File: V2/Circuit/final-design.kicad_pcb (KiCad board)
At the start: 2 copper layers, 62.8 x 62.2 mm, 27 parts, among them J1 Conn_02x05_Odd_Even, U1 LM338T, U2 TMC2209_SILENTSTEPSTICK

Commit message: minor changes in circuit and more dev in programming
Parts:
- renumbered StopButton1 to ControlSwitch1, ControlSwitch1 to StopButton1
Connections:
- ControlSwitch1 pad 1: STOP_Button -> control-mode-switch
- MCU1 pad 19: STOP_Button -> control-mode-switch
- MCU1 pad 21: control-mode-switch -> STOP_Button
- StopButton1 pad 1: control-mode-switch -> STOP_Button
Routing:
- net control-mode-switch: track 19.6 -> 6.91 mm
- net STOP_Button: track 6.91 -> 19.6 mm
- net GND: track 357.6 -> 356.7 mm
- net Encoder_button1: track 65.9 -> 66.6 mm

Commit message: minor circuit changes
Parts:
- R4: value 200 -> 150
- R5: value 330 -> 470
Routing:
- net Encoder_DT2: track 17.3 -> 16.2 mm
- net GND: track 356.7 -> 357.4 mm
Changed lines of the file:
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@@
 			)
 		)
-		(property "Value" "200"
+		(property "Value" "150"
 			(at 5.31 0 0)
 			(layer "F.Fab")
@@
 		)
 		(property "Value" "STC8H8K64U_SKDIP28"
-			(at 0.1 -21 0)
+			(at 0 0 90)
 			(unlocked yes)
 			(layer "F.Fab")
@@
 		)
 		(fp_text user "${REFERENCE}"
-			(at -0.2 -19.5 0)
+			(at 0.19 -15.99 0)
 			(unlocked yes)
 			(layer "F.Fab")
@@
 		)
 		(property "Value" "TMC2209_SILENTSTEPSTICK"
-			(at 11.05 11.115 0)
+			(at -1.15 -0.81 90)
 			(layer "F.Fab")
 			(effects
@@
 			)
 		)
-		(property "Value" "330"
+		(property "Value" "470"
 			(at 2.31 0 0)
 			(layer "F.Fab")
@@
 	)
 	(segment
-		(start 151.5 91.25)
-		(end 151.5 80.75)
-		(width 0.8)
-		(layer "F.Cu")
-		(net 1)
-	)
-	(segment
 		(start 121.529899 100.5)
 		(end 121.529899 100.499999)
@@
 	)
 	(segment
+		(start 151.3 91.75)
+		(end 145.669239 91.75)
+		(width 0.8)
+		(layer "F.Cu")
+		(net 1)
+	)
+	(segment
 		(start 146.75 114.25)
 		(end 146.25 114.75)
@@
 	)
 	(segment
-		(start 151.5 93.75)
-		(end 151.5 91.95)
+		(start 145.669239 91.75)
+		(end 143.869239 93.55)
 		(width 0.8)
 		(layer "F.Cu")
@@
 	)
 	(segment
-		(start 144.588478 91.75)
-		(end 142.788478 93.55)
-		(width 0.8)
-		(layer "F.Cu")
-		(net 1)
-	)
-	(segment
 		(start 105.916 95.166)
 		(end 104.95 94.2)
@@
 	)
 	(segment
+		(start 151.5 91.95)
+		(end 151.3 91.75)
+		(width 0.8)
+		(layer "F.Cu")
+		(net 1)
+	)
+	(segment
 		(start 119.75 113)
 		(end 122.69 113)
@@
 	)
 	(segment
+		(start 151.5 91.95)
+		(end 151.5 80.75)
+		(width 0.8)
+		(layer "F.Cu")
+		(net 1)
+	)
+	(segment
 		(start 104.05 76.34)
 		(end 105.65 74.74)
@@
 	)
 	(segment
-		(start 151.3 91.75)
-		(end 144.588478 91.75)
+		(start 134.75 69)
+		(end 136.137358 69)
 		(width 0.8)
 		(layer "F.Cu")
@@
 	)
 	(segment
-		(start 151.5 91.95)
-		(end 151.3 91.75)
+		(start 136.75 84.225)
+		(end 137.225 83.75)
 		(width 0.8)
 		(layer "F.Cu")
@@
 	)
 	(segment
-		(start 142.788478 93.55)
+		(start 143.869239 93.55)
 		(end 139.25 93.55)
 		(width 0.8)
@@
 	)
 	(segment
-		(start 134.75 69)
-		(end 136.137358 69)
-		(width 0.8)
-		(layer "F.Cu")
-		(net 1)
-	)
-	(segment
-		(start 136.75 84.225)
-		(end 137.225 83.75)
-		(width 0.8)
-		(layer "F.Cu")
-		(net 1)
-	)
-	(segment
 		(start 148.75 75.46)
 		(end 146.21 75.46)
@@
 	)
 	(segment
+		(start 151.5 93.75)
+		(end 151.5 91.95)
+		(width 0.8)
+		(layer "F.Cu")
+		(net 1)
+	)
+	(segment
 		(start 105.916 99.342956)
 		(end 105.916 95.166)
@@
 	)
 	(segment
+		(start 146.75 70.25)
+		(end 145.05 68.55)
+		(width 0.8)
+		(layer "F.Cu")
+		(net 14)
+	)
+	(segment
 		(start 104.065 70.35)
 		(end 104.065 69.159874)
@@
 	)
 	(segment
+		(start 145.05 68.55)
+		(end 138.425836 68.55)
+		(width 0.8)
+		(layer "F.Cu")
+		(net 14)
+	)
+	(segment
 		(start 141.76 82.45)
 		(end 136.55 82.45)
@@
 	)
 	(segment
-		(start 137.5 72.75)
-		(end 132.75 77.5)
-		(width 0.8)
-		(layer "F.Cu")
-		(net 14)
-	)
-	(segment
 		(start 121.17 62.70868)
 		(end 121.17 60.714466)
@@
 	)
 	(segment
-		(start 146.75 70.25)
-		(end 145.05 68.55)
-		(width 0.8)
-		(layer "F.Cu")
-		(net 14)
-	)
-	(segment
 		(start 122.62 107.38)
 		(end 123.23 107.38)
@@
 	)
 	(segment
-		(start 132.75 77.5)
-		(end 131.834415 77.5)
-		(width 0.8)
+		(start 117.87868 66)
+		(end 121.17 62.70868)
+		(width 1)
 		(layer "F.Cu")
 		(net 14)
 	)
 	(segment
-		(start 145.05 68.55)
-		(end 138.425836 68.55)
+		(start 138.425836 68.55)
+		(end 137.43 69.545836)
 		(width 0.8)
 		(layer "F.Cu")
@@
 	)
 	(segment
-		(start 117.87868 66)
-		(end 121.17 62.70868)
-		(width 1)
-		(layer "F.Cu")
-		(net 14)
-	)
-	(segment
 		(start 122.634466 59.25)
 		(end 124.705534 59.25)
@@
 	)
 	(segment
-		(start 104.065 69.159874)
-		(end 107.224874 66)
-		(width 1)
+		(start 137.43 72.82)
+		(end 132.75 77.5)
+		(width 0.8)
 		(layer "F.Cu")
 		(net 14)
 	)
 	(segment
-		(start 138.425836 68.55)
-		(end 137.43 69.545836)
-		(width 0.8)
+		(start 104.065 69.159874)
+		(end 107.224874 66)
+		(width 1)
 		(layer "F.Cu")
 		(net 14)
@@
 	)
 	(segment
-		(start 137.43 72.68)
-		(end 137.5 72.75)
-		(width 0.8)
-		(layer "F.Cu")
-		(net 14)
-	)
-	(segment
 		(start 124.705534 59.25)
 		(end 126.21 60.754466)
@@
 	)
 	(segment
+		(start 137.43 69.545836)
+		(end 137.43 72.82)
+		(width 0.8)
+		(layer "F.Cu")
+		(net 14)
+	)
+	(segment
 		(start 126.21 71.13)
 		(end 129.95 67.39)
@@
 	)
 	(segment
-		(start 137.43 69.545836)
-		(end 137.43 72.68)
+		(start 132.75 77.5)
+		(end 131.834415 77.5)
 		(width 0.8)
 		(layer "F.Cu")
@@
 	)
 	(segment
-		(start 130.85 89.6)
-		(end 131.951522 89.6)
-		(width 0.8)
-		(layer "F.Cu")
-		(net 15)
-	)
-	(segment

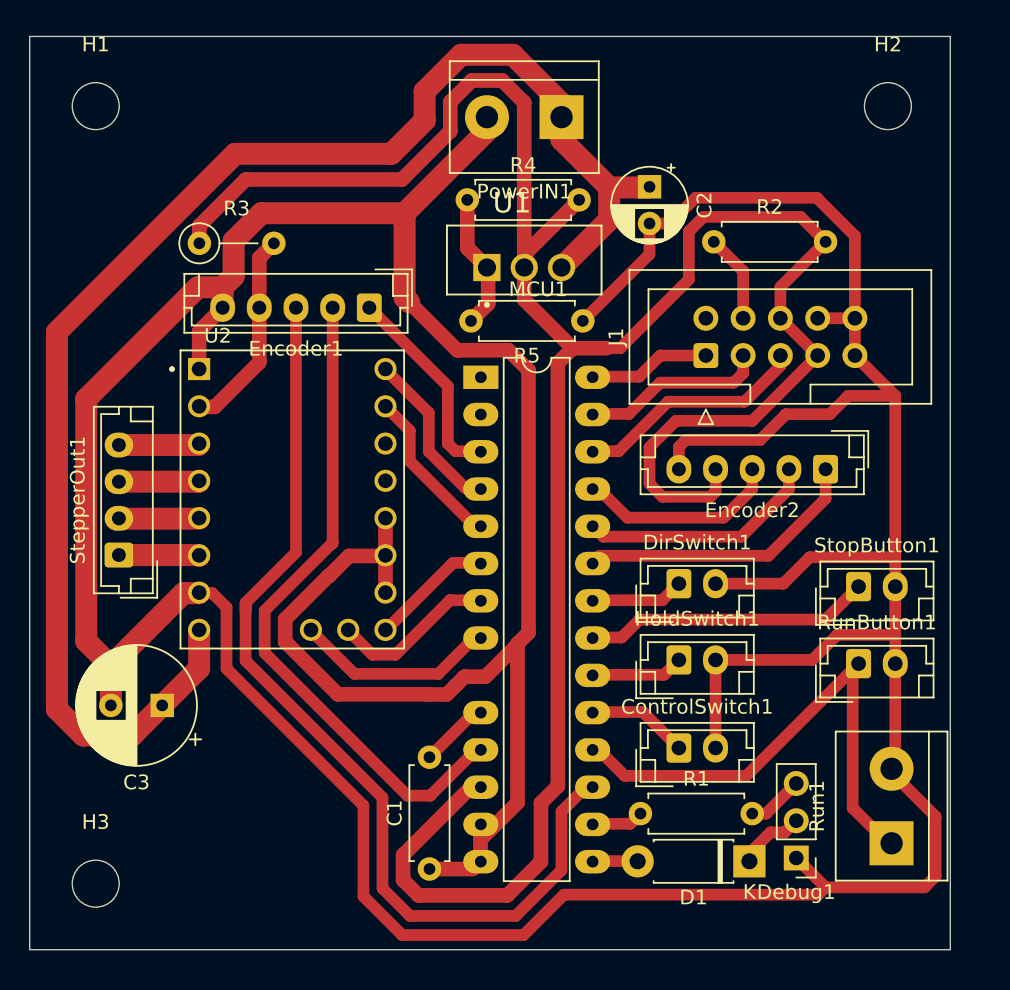
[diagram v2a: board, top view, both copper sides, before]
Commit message: upgraded board to use l7805 instead of lm317
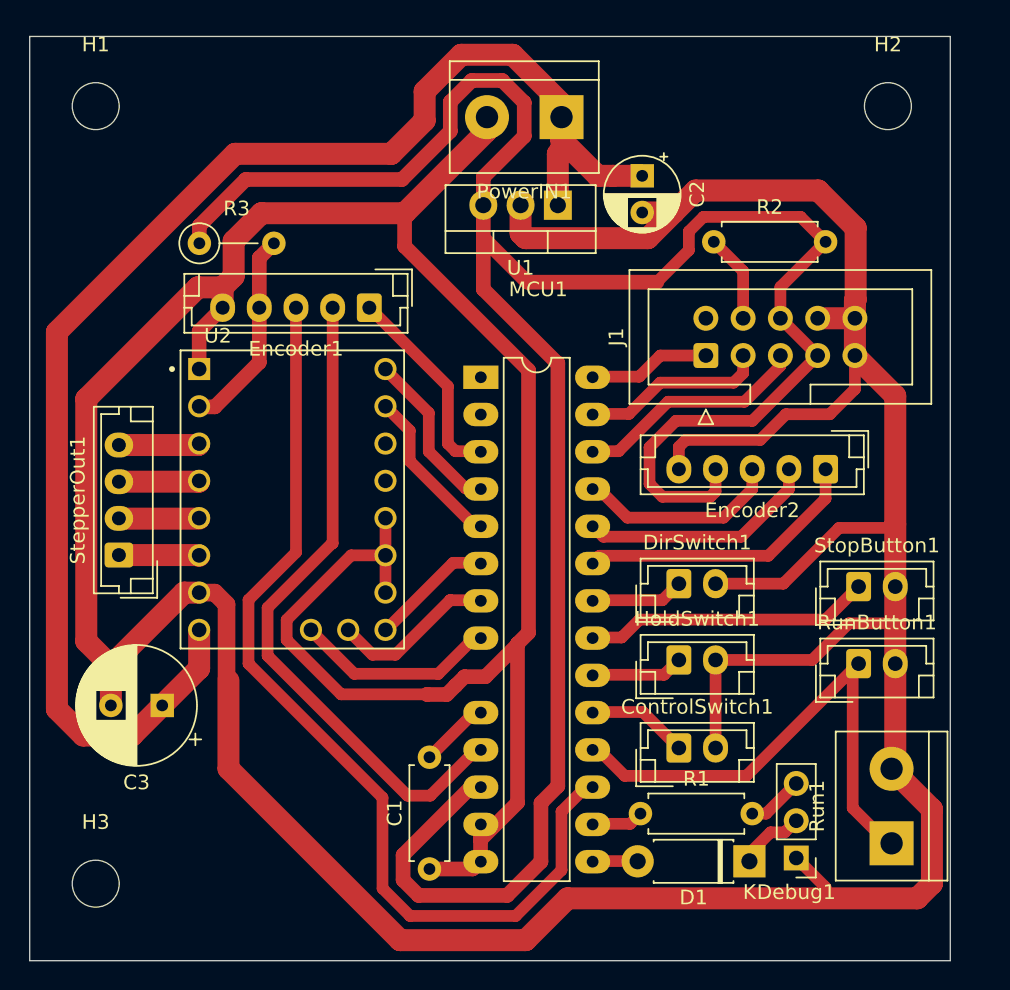
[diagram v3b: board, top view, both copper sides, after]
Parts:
- removed R4: 150, Resistor_THT:R_Axial_DIN0207_L6.3mm_D2.5mm_P7.62mm_Horizontal
- removed R5: 470, Resistor_THT:R_Axial_DIN0207_L6.3mm_D2.5mm_P7.62mm_Horizontal
- U1: value LM338T -> L7805; footprint LM338T:TO254P1054X470X1955-3 -> Package_TO_SOT_THT:TO-220-3_Vertical
- moved U1 4.83 mm to (128.5, 67.8), turned to 180 degrees
- moved C2 0.90 mm to (134.2, 65.8)
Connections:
- U1 pad 1: Net-(U1-ADJ) -> +24V
- U1 pad 2: +5V -> GND
- U1 pad 3: +24V -> +5V
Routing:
- net Net-(U1-ADJ): track 11.2 -> 0.00 mm
- net GND: track 357.4 -> 362.5 mm
- net +24V: track 102.0 -> 99.3 mm
- net Encoder_button1: track 66.6 -> 65.8 mm
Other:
- board size 62.8 x 62.2 mm -> 62.8 x 63 mm
